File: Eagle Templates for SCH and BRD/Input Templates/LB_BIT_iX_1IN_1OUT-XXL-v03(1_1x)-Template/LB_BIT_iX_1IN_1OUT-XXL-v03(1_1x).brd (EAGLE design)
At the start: 21.4 x 51.2 mm, 17 parts, among them U1 LV321SOT23-5, U2 LV321SOT23-5

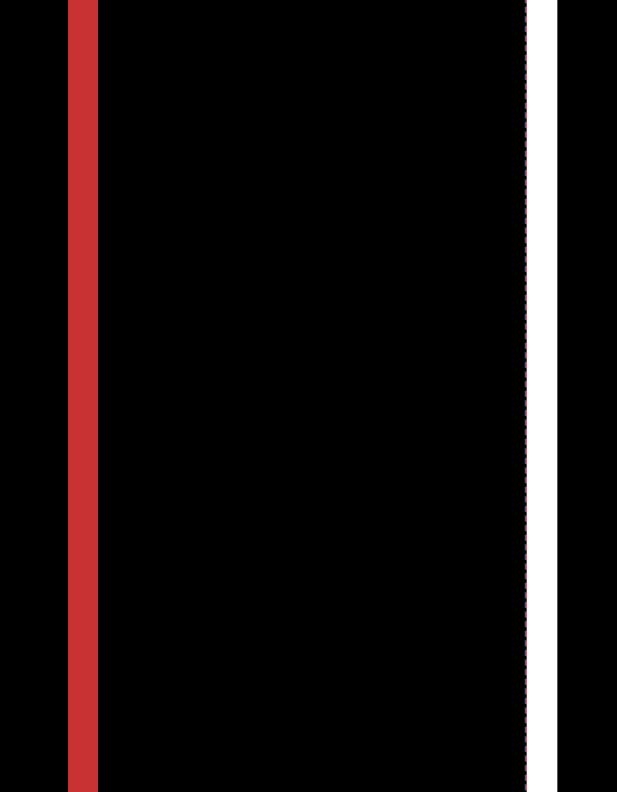
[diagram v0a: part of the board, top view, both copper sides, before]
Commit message: added bitlab logo and made minor changes to board templates. Updated littlebits library.
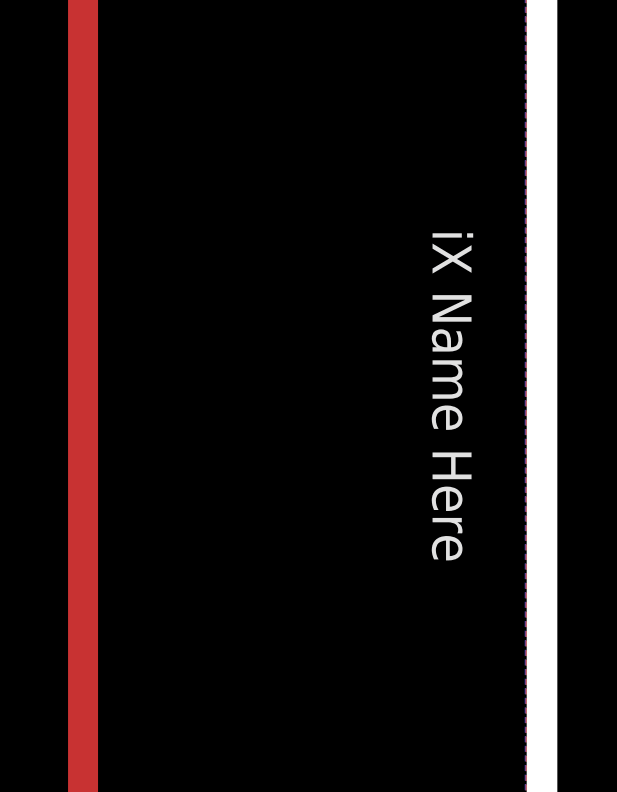
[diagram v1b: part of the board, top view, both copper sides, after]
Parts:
- added U$5: (no value), LITTLEBITS:BITLAB-LOGO
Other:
- board text added: "iX Name Here"
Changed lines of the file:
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@@
 <layer number="113" name="extra" color="10" fill="1" visible="yes" active="yes"/>
 <layer number="116" name="Patch_BOT" color="9" fill="4" visible="yes" active="yes"/>
+<layer number="118" name="Rect_Pads" color="7" fill="1" visible="no" active="yes"/>
 <layer number="121" name="_tsilk" color="7" fill="1" visible="yes" active="yes"/>
 <layer number="122" name="_bsilk" color="7" fill="1" visible="yes" active="yes"/>
@@
 <wire x1="23.91" y1="55.335" x2="23.91" y2="4.11" width="1" layer="46"/>
 <wire x1="20.785" y1="55.335" x2="23.91" y2="55.335" width="1" layer="46"/>
+<text x="20.9" y="29.9" size="1.3" layer="21" font="vector" rot="SR270" align="center">iX Name Here</text>
 </plain>
 <attributes>
@@
 <element name="U$4" library="ohw-logo" package="OSHW_FILLX150_NOTEXT" value="" x="18.9" y="49.5" rot="MR90"/>
 <element name="U$1" library="LITTLEBITS" package="FABDWG01-OHW" value="FRAME-LETTER" x="0" y="0"/>
+<element name="U$5" library="LITTLEBITS" package="BITLAB-LOGO" value="" x="19.2" y="34" rot="R270"/>
 </elements>
 <signals>

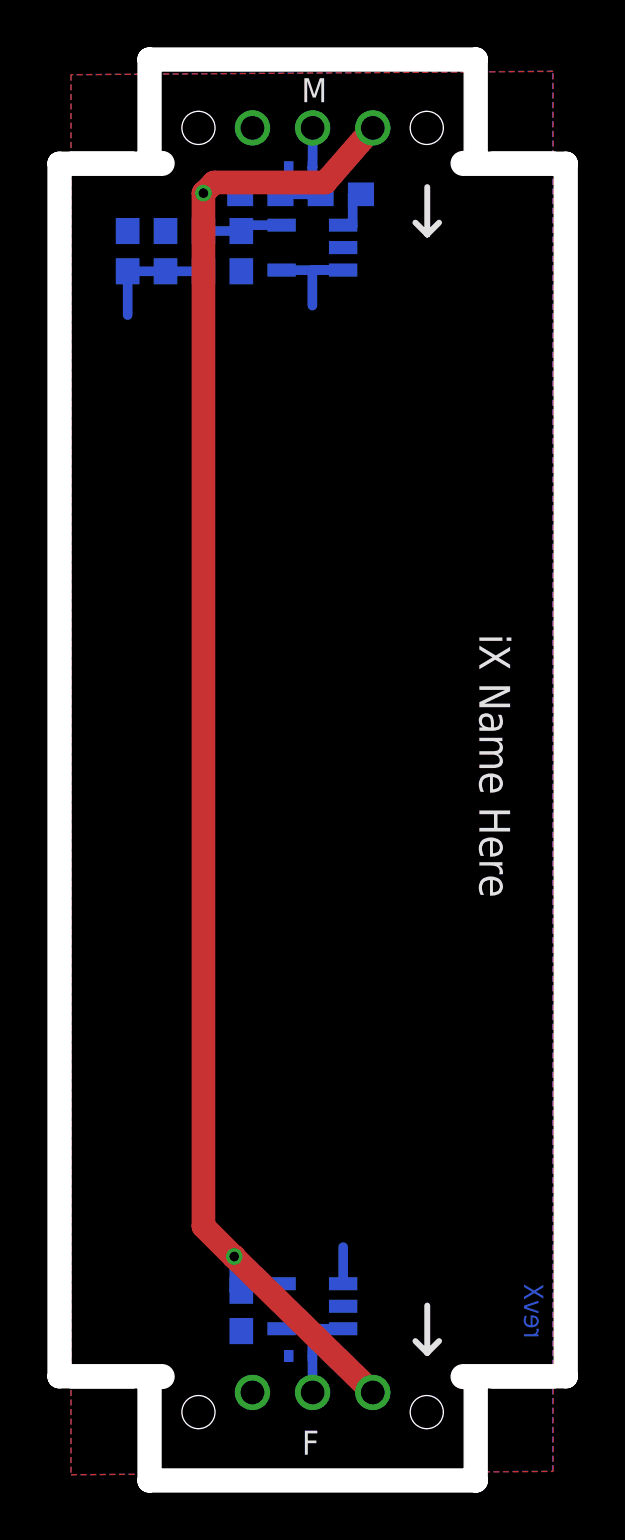
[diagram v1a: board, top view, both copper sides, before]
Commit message: Updated templates
- Added ferrite beads
- Moved text and annotations off of Nets layer
- Minor layout changes
- Removed I/O/W prefix from reference designators
- Removed output stage components from output bits
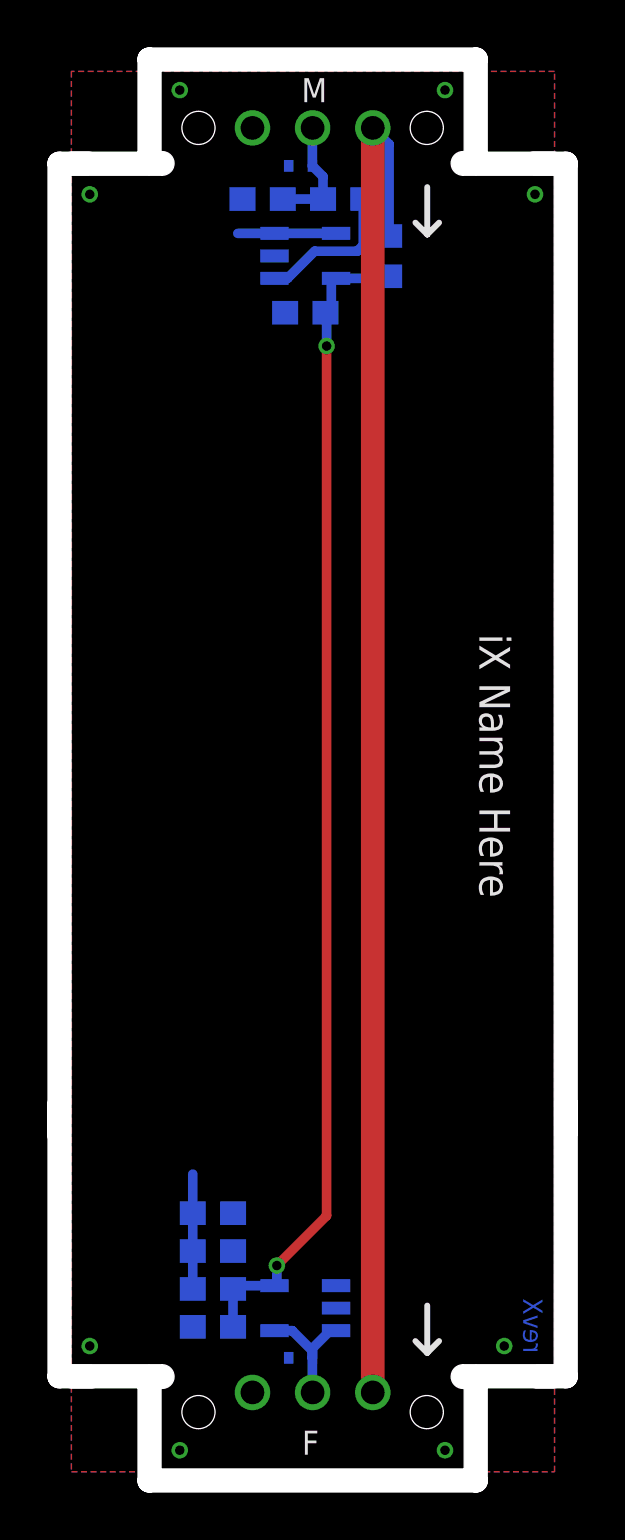
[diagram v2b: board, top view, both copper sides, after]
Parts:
- removed I?C1: 0.1uF, LITTLEBITS:CAP-0603
- removed I?C2: 10uF, LITTLEBITS:CAP-0603
- removed I?C3: 1.0uF, LITTLEBITS:CAP-0603
- removed I?R1: 1meg, LITTLEBITS:RES-0603
- removed I?R2: 10K, LITTLEBITS:RES-0603
- removed I?R3, I?R4: 3K3, LITTLEBITS:RES-0603
- removed I?TVS1, I?TVS2: ESD9B5.0ST5G, LITTLEBITS:SOD-923
- added C1: 0.1uF, LITTLEBITS:CAP-0603
- added C2: 10uF, LITTLEBITS:CAP-0603
- added C3: 1.0uF, LITTLEBITS:CAP-0603
- added FB1: FERRITE-BEAD0603, LITTLEBITS:R0603
- added R1: 1meg, LITTLEBITS:RES-0603
- added R2: 10K, LITTLEBITS:RES-0603
- added R3, R4: 3K3, LITTLEBITS:RES-0603
- added TVS1, TVS2: ESD9B5.0ST5G, LITTLEBITS:SOD-923
- U$1: value FRAME-LETTER -> OSHW-LOGOL; device LITTLEBITS:FABDWG01-OHW -> LITTLEBITS131206:OSHW-LOGO-L
- U$2: value OSHW-LOGOL -> OSHWCREDIT; device LITTLEBITS131206:OSHW-LOGO-L -> LITTLEBITS:OSHWCREDIT
- U$3: value OSHWCREDIT -> FRAME-LETTER; device LITTLEBITS:OSHWCREDIT -> LITTLEBITS:FABDWG01-OHW
- moved U$3 111.7 mm to (0.00, 0.00)
- moved U$1 77.8 mm to (-37.5, -68.2)
- moved U$2 65.8 mm to (-92.2, -64.3)
- moved U1 0.46 mm to (12.9, 51.4), turned to 90 degrees
- moved U2 0.31 mm to (12.9, 7.00)
- renumbered I?BSF to BSF1, I?BSM to BSM1
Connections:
- new net LB_VCC: BSF1.VCC, BSM1.VCC1, FB1.2
- net GND: now also C1.2, C2.2, C3.1, R1.1, R4.1, TVS1.1, TVS2.1; no longer I?C1.2, I?C2.2, I?C3.1, I?R1.1, I?R4.1, I?TVS1.1, I?TVS2.1
- net N$4: now also R2.1; no longer I?R2.1
- net SIG_IN: now also R1.2, R2.2, TVS1.2; no longer I?R1.2, I?R2.2, I?TVS1.2
- net SIG_OUT: now also TVS2.2; no longer I?TVS2.2
- net VCC: now also C1.1, C3.2, FB1.1, R3.2; no longer BSF1.VCC, BSM1.VCC1, I?C1.1, I?C3.2, I?R3.2
- net VREF: now also C2.1, R3.1, R4.2; no longer I?C2.1, I?R3.1, I?R4.2
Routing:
- net LB_VCC: track 0.00 -> 58.2 mm
- net VCC: track 71.0 -> 50.1 mm
- net N$4: track 2.10 -> 6.28 mm
- net N$3: track 1.55 -> 0.00 mm
- net N$2: track 5.40 -> 4.15 mm
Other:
- outline, holes or cut-outs redrawn
